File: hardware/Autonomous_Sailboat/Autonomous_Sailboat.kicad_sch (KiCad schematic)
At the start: 16 parts, among them Q1 Q_NMOS, U1 STM32H755ZITx

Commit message: schematic update
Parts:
- R_B2-: value 82k -> 18k
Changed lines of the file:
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@@
 			)
 		)
-		(property "Value" "82k"
+		(property "Value" "18k"
 			(at 396.24 134.6199 0)
 			(effects

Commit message: naive battery monitor
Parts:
- removed C_filterB1: 100nF, symbol Device:C
- added C_filterB2: 100nF, symbol Device:C
- renumbered C_filterB2 to C_filterB1
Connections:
- net GND: now also C_filterB1.1, C_filterB3.1, C_filterB4.1, C_filterB2.1
- net at C_filterB3.2, R_B3+.2, R_B3-.1: now also U1.43 (PA4)
- net at R_B1+.2, R_B1-.1: now also C_filterB1.2, U1.37 (PA0)
- net at C_filterB4.2, R_B4+.2, R_B4-.1: now also U1.44 (PA5)
- net at U1.38 (PA1): now also R_B2+.2, R_B2-.1, C_filterB2.2; no longer C_filterB1.1
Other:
- moved on the sheet: C_filterB1

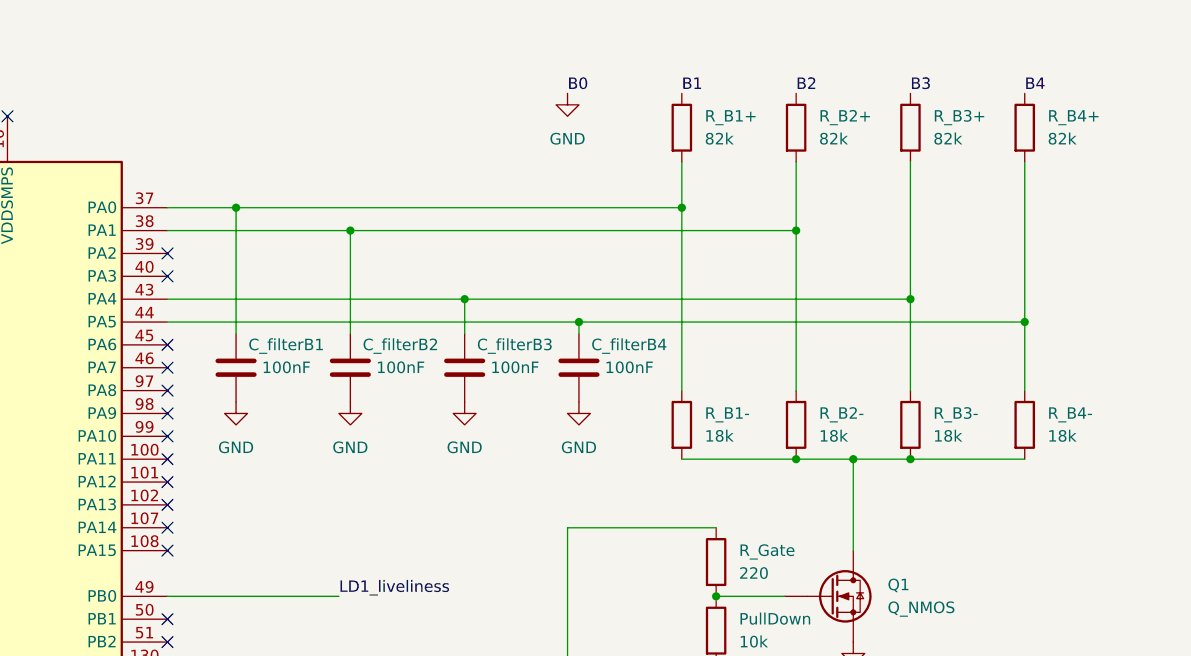
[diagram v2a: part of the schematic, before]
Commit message: Now the battery monitor is reading correctly
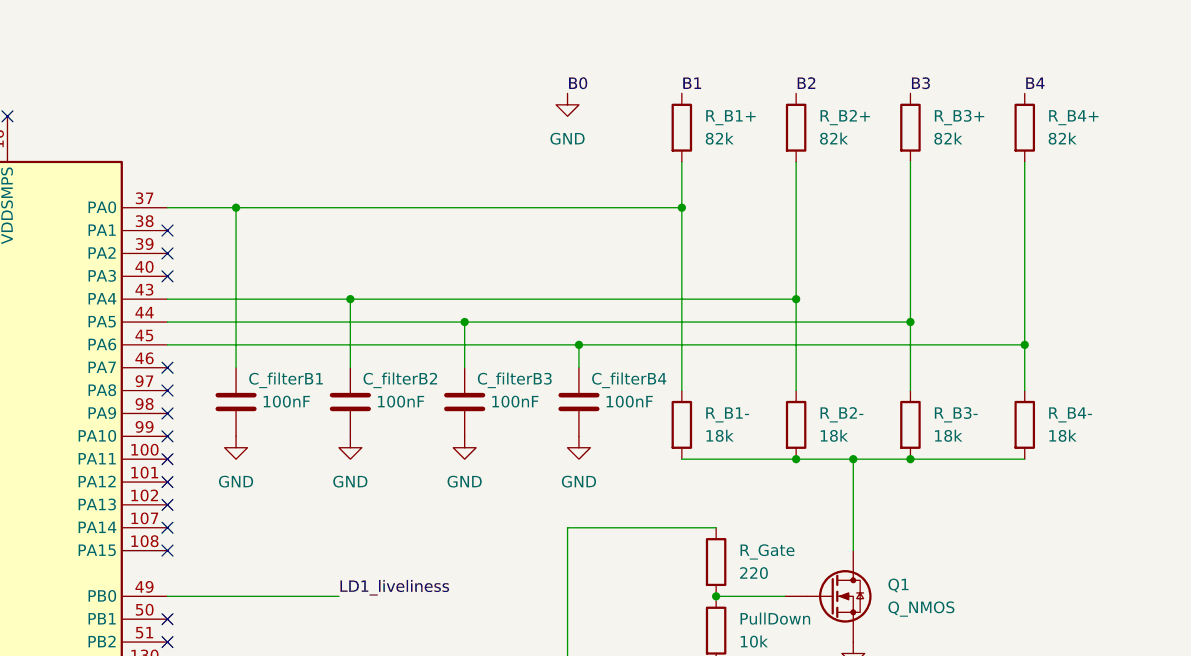
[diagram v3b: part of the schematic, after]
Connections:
- net at C_filterB3.2, R_B3+.2, R_B3-.1: now also U1.44 (PA5); no longer U1.43 (PA4)
- net at C_filterB2.2, R_B2+.2, R_B2-.1: now also U1.43 (PA4); no longer U1.38 (PA1)
- net at C_filterB4.2, R_B4+.2, R_B4-.1: now also U1.45 (PA6); no longer U1.44 (PA5)
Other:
- moved on the sheet: C_filterB1, C_filterB2, C_filterB3, C_filterB4
